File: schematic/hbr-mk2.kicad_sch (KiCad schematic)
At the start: 34 parts, among them J1 Barrel_Jack, J3 AudioJack3, Q1 IRF4905, Q2 2N7000, Q3 2N7000, Q4 IRF4905, SW1 SW_SPST, SW10 SW_Push, SW11 RotaryEncoder_Switch, SW2 SW_SPST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

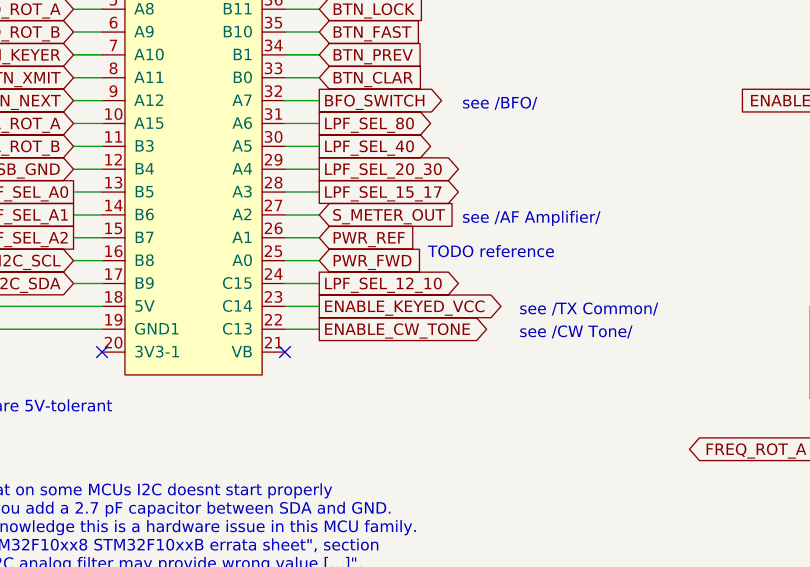
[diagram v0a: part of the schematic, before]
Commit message: Schematic: add relays to /LPFs/ sheet
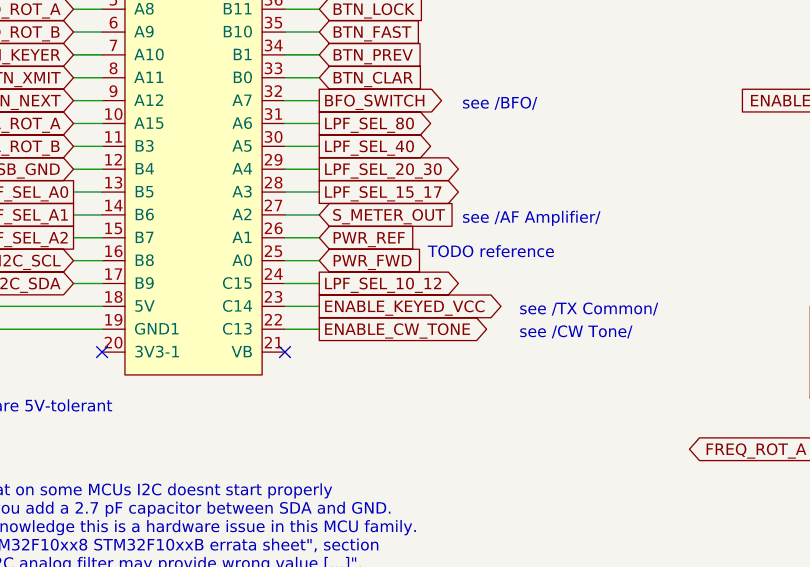
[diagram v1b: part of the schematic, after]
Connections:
- net LPF_SEL_12_10 renamed LPF_SEL_10_12
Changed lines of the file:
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@@
     )
   )
-  (global_label "LPF_SEL_12_10" (shape output) (at 160.655 104.775 0) (fields_autoplaced)
+  (global_label "LPF_SEL_10_12" (shape output) (at 160.655 104.775 0) (fields_autoplaced)
     (effects (font (size 1.27 1.27)) (justify left))
     (property "Intersheetrefs" "${INTERSHEET_REFS}" (at 178.0749 104.775 0)

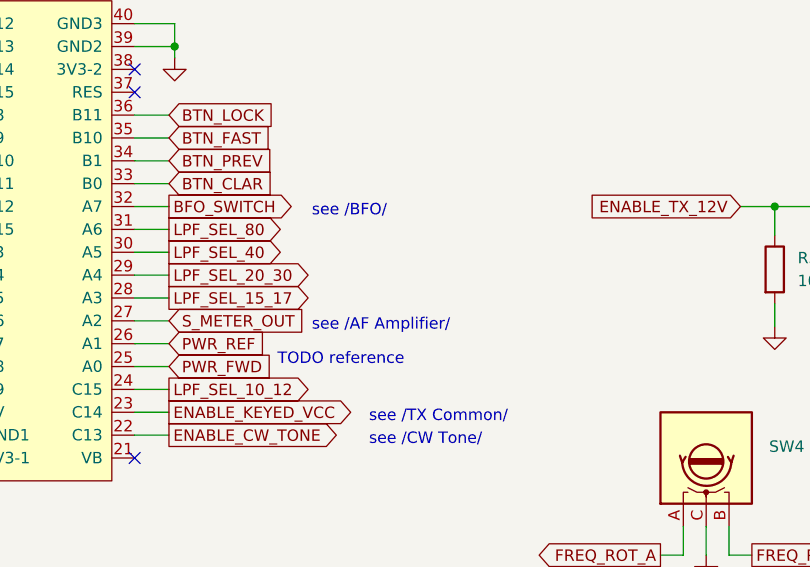
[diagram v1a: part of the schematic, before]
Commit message: Schematic: minor changes
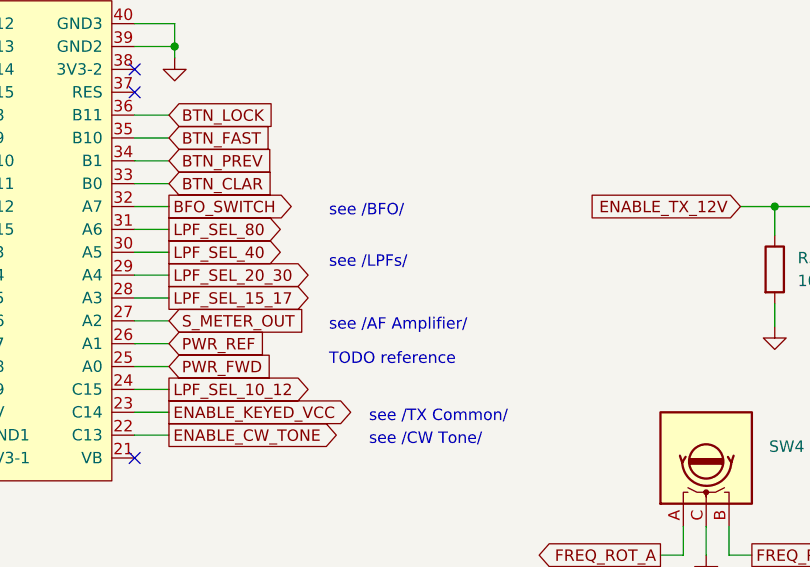
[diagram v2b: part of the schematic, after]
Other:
- note added: "see /LPFs/"
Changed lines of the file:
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@@
     (stroke (width 0) (type default))
   )
-  (text "TODO reference" (at 172.72 102.235 0)
+  (text "TODO reference" (at 178.435 102.235 0)
     (effects (font (size 1.27 1.27)) (justify left bottom))
   )
@@
     (effects (font (size 1.27 1.27)) (justify left bottom))
   )
-  (text "see /AF Amplifier/" (at 176.53 98.425 0)
+  (text "see /AF Amplifier/" (at 178.435 98.425 0)
     (effects (font (size 1.27 1.27)) (justify left bottom))
   )
   (text "see /Xtal Filters/" (at 169.545 155.575 0)
+    (effects (font (size 1.27 1.27)) (justify left bottom))
+  )
+  (text "see /LPFs/" (at 178.435 91.44 0)
     (effects (font (size 1.27 1.27)) (justify left bottom))
   )
@@
     (effects (font (size 1.27 1.27)) (justify left bottom))
   )
-  (text "see /BFO/" (at 176.53 85.725 0)
+  (text "see /BFO/" (at 178.435 85.725 0)
     (effects (font (size 1.27 1.27)) (justify left bottom))
   )

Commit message: Minor changes
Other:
- moved on the sheet: U3, U4

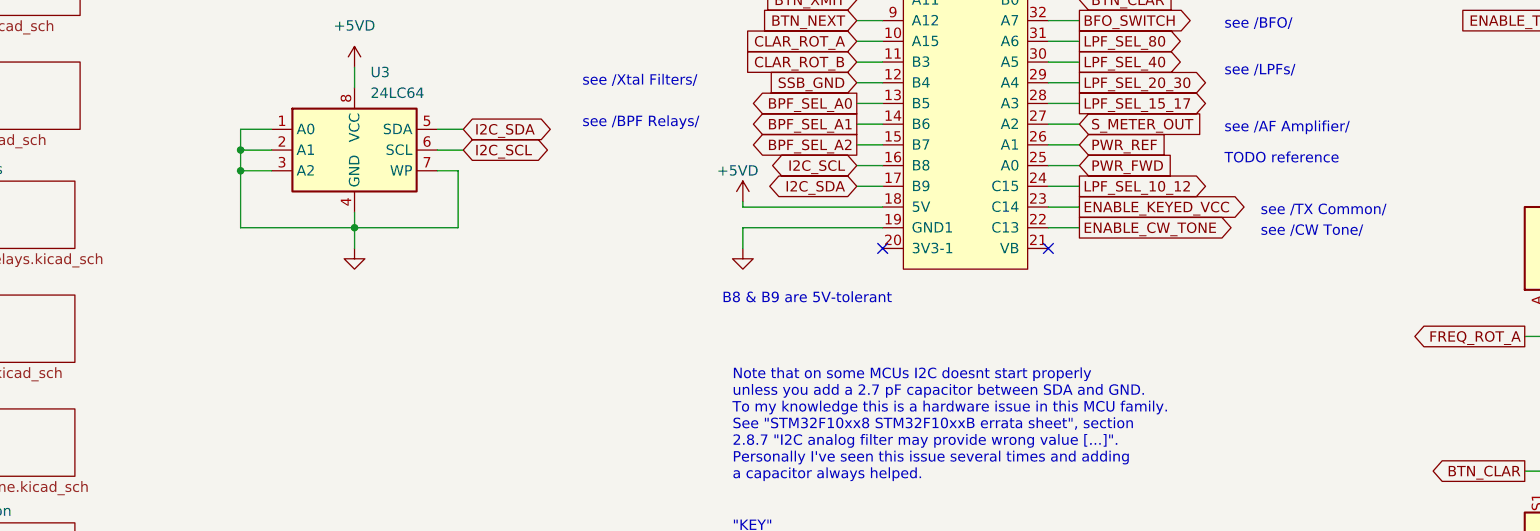
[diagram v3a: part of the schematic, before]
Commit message: Schematic: add SWR bridge
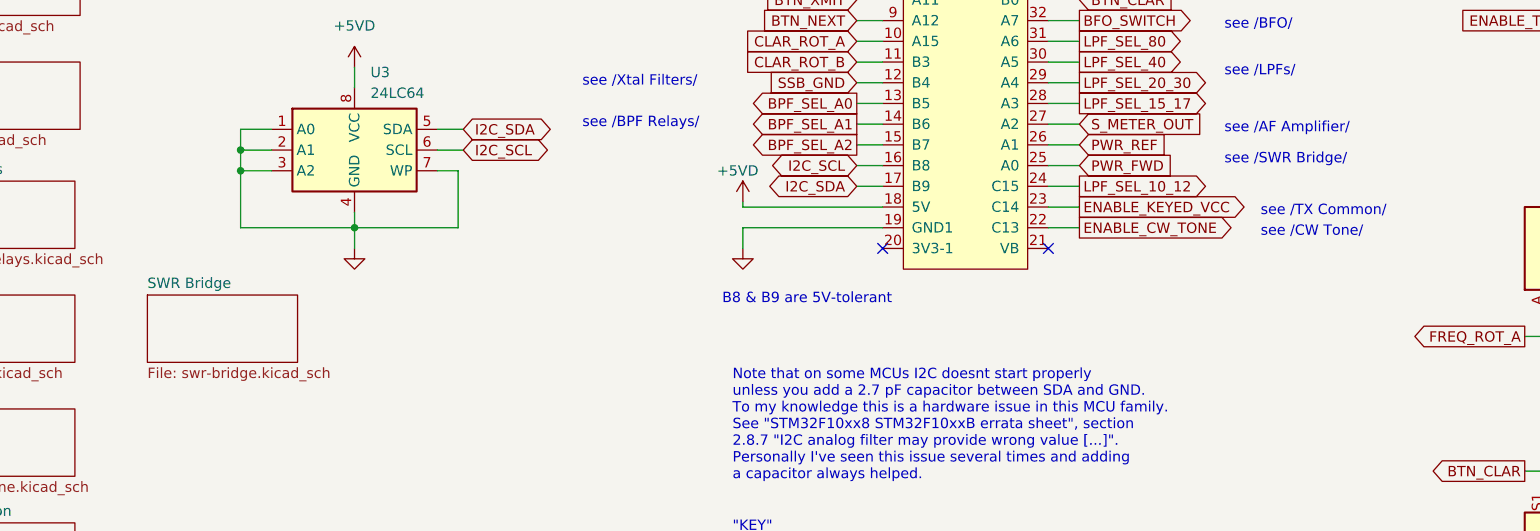
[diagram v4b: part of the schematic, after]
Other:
- added sheet SWR Bridge (swr-bridge.kicad_sch)
- note added: "see /SWR Bridge/"
- note removed: "TODO reference"
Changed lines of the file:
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@@
     (stroke (width 0) (type default))
   )
-  (text "TODO reference" (at 178.435 102.235 0)
+  (text "see /SWR Bridge/" (at 178.435 102.235 0)
     (effects (font (size 1.27 1.27)) (justify left bottom))
   )
@@
       )
     )
+  )
+  (sheet (at 46.355 118.11) (size 18.415 8.255) (fields_autoplaced)
+    (stroke (width 0.1524) (type solid))
+    (fill (color 0 0 0 0.0000))
+    (property "Sheetname" "SWR Bridge" (at 46.355 117.3984 0)
+      (effects (font (size 1.27 1.27)) (justify left bottom))
+    )
+    (property "Sheetfile" "swr-bridge.kicad_sch" (at 46.355 126.9496 0)
+      (effects (font (size 1.27 1.27)) (justify left top))
+    )
+    (instances
+      (project "hbr-mk2"
+        (path "/700c9878-4ed7-49d5-a273-77cf9d92989d" (page "14"))
+      )
+    )

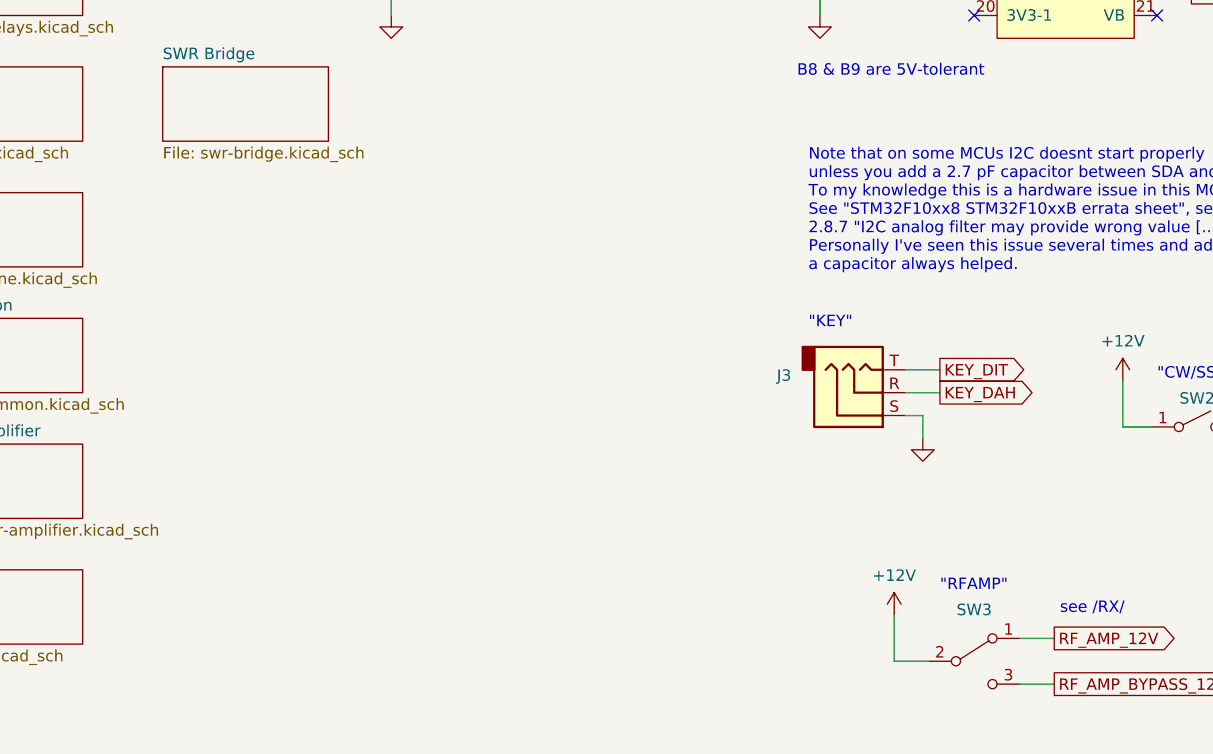
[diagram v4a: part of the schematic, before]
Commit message: Add /TX SSB/ sheet
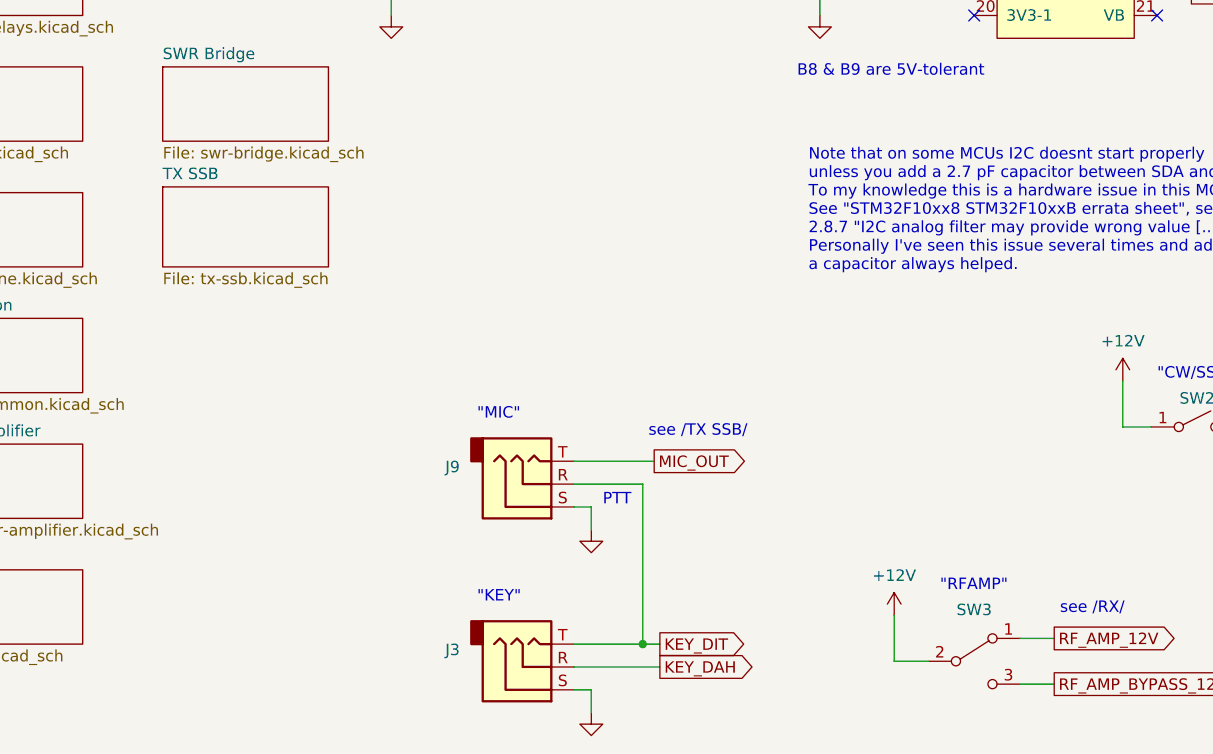
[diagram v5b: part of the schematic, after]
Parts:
- added J9: AudioJack3, symbol Connector_Audio:AudioJack3
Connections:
- net GND: now also J9.S
- net KEY_DIT: now also J9.R
- new net MIC_OUT: J9.T
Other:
- added sheet TX SSB (tx-ssb.kicad_sch)
- note added: ""MIC""
- note added: "PTT"
- note added: "see /TX SSB/"
- moved on the sheet: J3
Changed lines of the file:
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@@
   (junction (at 74.295 32.385) (diameter 0) (color 0 0 0 0)
+  )
+  (junction (at 99.695 182.245) (diameter 0) (color 0 0 0 0)
   )
   (junction (at 255.27 76.2) (diameter 0) (color 0 0 0 0)
@@
     (stroke (width 0) (type default))
   )
+  (wire (pts (xy 99.695 182.245) (xy 101.6 182.245))
+    (stroke (width 0) (type default))
+  )
   (wire (pts (xy 225.425 123.19) (xy 222.885 123.19))
     (stroke (width 0) (type default))
@@
     (stroke (width 0) (type default))
   )
-  (wire (pts (xy 128.905 151.765) (xy 132.715 151.765))
+  (wire (pts (xy 92.075 182.245) (xy 99.695 182.245))
     (stroke (width 0) (type default))
   )
@@
     (stroke (width 0) (type default))
   )
+  (wire (pts (xy 93.98 169.545) (xy 93.98 167.005))
+    (stroke (width 0) (type default))
+  )
   (wire (pts (xy 74.295 32.385) (xy 74.295 34.925))
     (stroke (width 0) (type default))
@@
     (stroke (width 0) (type default))
   )
-  (wire (pts (xy 130.81 159.385) (xy 130.81 156.845))
+  (wire (pts (xy 93.98 189.865) (xy 93.98 187.325))
     (stroke (width 0) (type default))
   )
@@
     (stroke (width 0) (type default))
   )
-  (wire (pts (xy 130.81 156.845) (xy 128.905 156.845))
+  (wire (pts (xy 93.98 187.325) (xy 92.075 187.325))
     (stroke (width 0) (type default))
   )
@@
     (stroke (width 0) (type default))
   )
+  (wire (pts (xy 92.075 164.465) (xy 99.695 164.465))
+    (stroke (width 0) (type default))
+  )
   (wire (pts (xy 74.295 42.545) (xy 74.295 45.085))
     (stroke (width 0) (type default))
@@
     (stroke (width 0) (type default))
   )
+  (wire (pts (xy 93.98 167.005) (xy 92.075 167.005))
+    (stroke (width 0) (type default))
+  )
   (wire (pts (xy 133.35 94.615) (xy 136.525 94.615))
     (stroke (width 0) (type default))
@@
     (stroke (width 0) (type default))
   )
+  (wire (pts (xy 92.075 161.925) (xy 100.965 161.925))
+    (stroke (width 0) (type default))
+  )
   (wire (pts (xy 220.345 157.48) (xy 220.345 160.655))
     (stroke (width 0) (type default))
@@
     (stroke (width 0) (type default))
   )
+  (wire (pts (xy 99.695 164.465) (xy 99.695 182.245))
+    (stroke (width 0) (type default))
+  )
   (wire (pts (xy 255.27 36.83) (xy 255.27 39.37))
     (stroke (width 0) (type default))
@@
     (stroke (width 0) (type default))
   )
-  (wire (pts (xy 128.905 154.305) (xy 132.715 154.305))
+  (wire (pts (xy 92.075 184.785) (xy 101.6 184.785))
     (stroke (width 0) (type default))
   )
@@
     (effects (font (size 1.27 1.27)) (justify left bottom))
   )
+  (text "see /TX SSB/" (at 100.33 159.385 0)
+    (effects (font (size 1.27 1.27)) (justify left bottom))
+  )
   (text "\"13.8V\"" (at 54.61 27.305 0)
+    (effects (font (size 1.27 1.27)) (justify left bottom))
+  )
+  (text "PTT" (at 95.25 167.005 0)
     (effects (font (size 1.27 1.27)) (justify left bottom))
   )
@@
     (effects (font (size 1.27 1.27)) (justify left bottom))
   )
+  (text "\"MIC\"" (at 81.28 157.48 0)
+    (effects (font (size 1.27 1.27)) (justify left bottom))
+  )
   (text "see /TX Common/" (at 182.88 108.585 0)
     (effects (font (size 1.27 1.27)) (justify left bottom))
@@
     (effects (font (size 1.27 1.27)) (justify left bottom))
   )
-  (text "\"KEY\"" (at 118.11 147.32 0)
+  (text "\"KEY\"" (at 81.28 177.8 0)
     (effects (font (size 1.27 1.27)) (justify left bottom))
   )
@@
     )
   )
+  (global_label "MIC_OUT" (shape output) (at 100.965 161.925 0) (fields_autoplaced)
+    (effects (font (size 1.27 1.27)) (justify left))
+    (property "Intersheetrefs" "${INTERSHEET_REFS}" (at 111.7932 161.925 0)
+      (effects (font (size 1.27 1.27)) (justify left) hide)
+    )
+  )
   (global_label "SSB_12V" (shape output) (at 169.545 158.115 0) (fields_autoplaced)
     (effects (font (size 1.27 1.27)) (justify left))
@@
     )
   )
-  (global_label "KEY_DAH" (shape output) (at 132.715 154.305 0) (fields_autoplaced)
+  (global_label "KEY_DAH" (shape output) (at 101.6 184.785 0) (fields_autoplaced)
     (effects (font (size 1.27 1.27)) (justify left))
-    (property "Intersheetrefs" "${INTERSHEET_REFS}" (at 143.7851 154.305 0)
+    (property "Intersheetrefs" "${INTERSHEET_REFS}" (at 112.6701 184.785 0)
       (effects (font (size 1.27 1.27)) (justify left) hide)
     )
@@
     )
   )
-  (global_label "KEY_DIT" (shape output) (at 132.715 151.765 0) (fields_autoplaced)
+  (global_label "KEY_DIT" (shape output) (at 101.6 182.245 0) (fields_autoplaced)
     (effects (font (size 1.27 1.27)) (justify left))
-    (property "Intersheetrefs" "${INTERSHEET_REFS}" (at 142.9384 151.765 0)
+    (property "Intersheetrefs" "${INTERSHEET_REFS}" (at 111.8234 182.245 0)
       (effects (font (size 1.27 1.27)) (justify left) hide)
     )
@@
     )
   )
+  (symbol (lib_id "power:GND") (at 93.98 169.545 0) (unit 1)
+    (in_bom yes) (on_board yes) (dnp no) (fields_autoplaced)
+    (property "Reference" "#PWR0319" (at 93.98 175.895 0)
+      (effects (font (size 1.27 1.27)) hide)
+    )
+    (property "Value" "GND" (at 93.98 174.625 0)
+      (effects (font (size 1.27 1.27)) hide)
+    )
+    (property "Footprint" "" (at 93.98 169.545 0)
+      (effects (font (size 1.27 1.27)) hide)
+    )
+    (property "Datasheet" "" (at 93.98 169.545 0)
+      (effects (font (size 1.27 1.27)) hide)
+    )
+    (pin "1")
+    (instances
+      (project "hbr-mk2"
+        (path "/700c9878-4ed7-49d5-a273-77cf9d92989d"
+          (reference "#PWR0319") (unit 1)
+        )
+      )
+    )
+  )
   (symbol (lib_id "power:GND") (at 157.48 45.085 0) (unit 1)
     (in_bom yes) (on_board yes) (dnp no) (fields_autoplaced)
@@
         (path "/700c9878-4ed7-49d5-a273-77cf9d92989d"
           (reference "#PWR05") (unit 1)
+        )
+      )
+    )
+  )
+  (symbol (lib_id "Connector_Audio:AudioJack3") (at 86.995 164.465 0) (mirror x) (unit 1)
+    (in_bom yes) (on_board yes) (dnp no) (fields_autoplaced)
+    (property "Reference" "J9" (at 79.375 162.56 0)
+      (effects (font (size 1.27 1.27)) (justify right))
+    )
+    (property "Value" "AudioJack3" (at 79.375 165.1 0)
+      (effects (font (size 1.27 1.27)) (justify right) hide)
+    )
+    (property "Footprint" "" (at 86.995 164.465 0)
+      (effects (font (size 1.27 1.27)) hide)
+    )
+    (property "Datasheet" "~" (at 86.995 164.465 0)
+      (effects (font (size 1.27 1.27)) hide)
+    )
+    (pin "R")
+    (pin "S")
+    (pin "T")
+    (instances
+      (project "hbr-mk2"
+        (path "/700c9878-4ed7-49d5-a273-77cf9d92989d"
+          (reference "J9") (unit 1)
         )
       )
@@
     )
   )
-  (symbol (lib_id "Connector_Audio:AudioJack3") (at 123.825 154.305 0) (mirror x) (unit 1)
-    (in_bom yes) (on_board yes) (dnp no) (fields_autoplaced)
-    (property "Reference" "J3" (at 116.205 152.4 0)
+  (symbol (lib_id "Connector_Audio:AudioJack3") (at 86.995 184.785 0) (mirror x) (unit 1)
+    (in_bom yes) (on_board yes) (dnp no) (fields_autoplaced)
+    (property "Reference" "J3" (at 79.375 182.88 0)
       (effects (font (size 1.27 1.27)) (justify right))
     )
-    (property "Value" "AudioJack3" (at 116.205 154.94 0)
-      (effects (font (size 1.27 1.27)) (justify right) hide)
-    )
-    (property "Footprint" "" (at 123.825 154.305 0)
-      (effects (font (size 1.27 1.27)) hide)
-    )
-    (property "Datasheet" "~" (at 123.825 154.305 0)
+    (property "Value" "AudioJack3" (at 79.375 185.42 0)
+      (effects (font (size 1.27 1.27)) (justify right) hide)
+    )
+    (property "Footprint" "" (at 86.995 184.785 0)
+      (effects (font (size 1.27 1.27)) hide)
+    )
+    (property "Datasheet" "~" (at 86.995 184.785 0)
       (effects (font (size 1.27 1.27)) hide)
     )
@@
     )
   )
-  (symbol (lib_id "power:GND") (at 130.81 159.385 0) (unit 1)
-    (in_bom yes) (on_board yes) (dnp no) (fields_autoplaced)
-    (property "Reference" "#PWR0208" (at 130.81 165.735 0)
-      (effects (font (size 1.27 1.27)) hide)
-    )
-    (property "Value" "GND" (at 130.81 164.465 0)
-      (effects (font (size 1.27 1.27)) hide)
-    )
-    (property "Footprint" "" (at 130.81 159.385 0)
-      (effects (font (size 1.27 1.27)) hide)
-    )
-    (property "Datasheet" "" (at 130.81 159.385 0)
+  (symbol (lib_id "power:GND") (at 93.98 189.865 0) (unit 1)
+    (in_bom yes) (on_board yes) (dnp no) (fields_autoplaced)
+    (property "Reference" "#PWR0208" (at 93.98 196.215 0)
+      (effects (font (size 1.27 1.27)) hide)
+    )
+    (property "Value" "GND" (at 93.98 194.945 0)
+      (effects (font (size 1.27 1.27)) hide)
+    )
+    (property "Footprint" "" (at 93.98 189.865 0)
+      (effects (font (size 1.27 1.27)) hide)
+    )
+    (property "Datasheet" "" (at 93.98 189.865 0)
       (effects (font (size 1.27 1.27)) hide)
     )
@@
       )
     )
+  )
+  (sheet (at 46.355 131.445) (size 18.415 8.89) (fields_autoplaced)
+    (stroke (width 0.1524) (type solid))
+    (fill (color 0 0 0 0.0000))
+    (property "Sheetname" "TX SSB" (at 46.355 130.7334 0)
+      (effects (font (size 1.27 1.27)) (justify left bottom))
+    )
+    (property "Sheetfile" "tx-ssb.kicad_sch" (at 46.355 140.9196 0)
+      (effects (font (size 1.27 1.27)) (justify left top))
+    )
+    (instances
+      (project "hbr-mk2"
+        (path "/700c9878-4ed7-49d5-a273-77cf9d92989d" (page "15"))
+      )
+    )
